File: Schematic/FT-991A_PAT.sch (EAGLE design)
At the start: 30 parts, among them Q1 PE4259, Q2 MC78L09ABDR2GOSCT, Q5 NCP553, Q7 J310, Q8 5086, X1 IF_IN, X2 SCP_OUT, X3 SDR_OUT

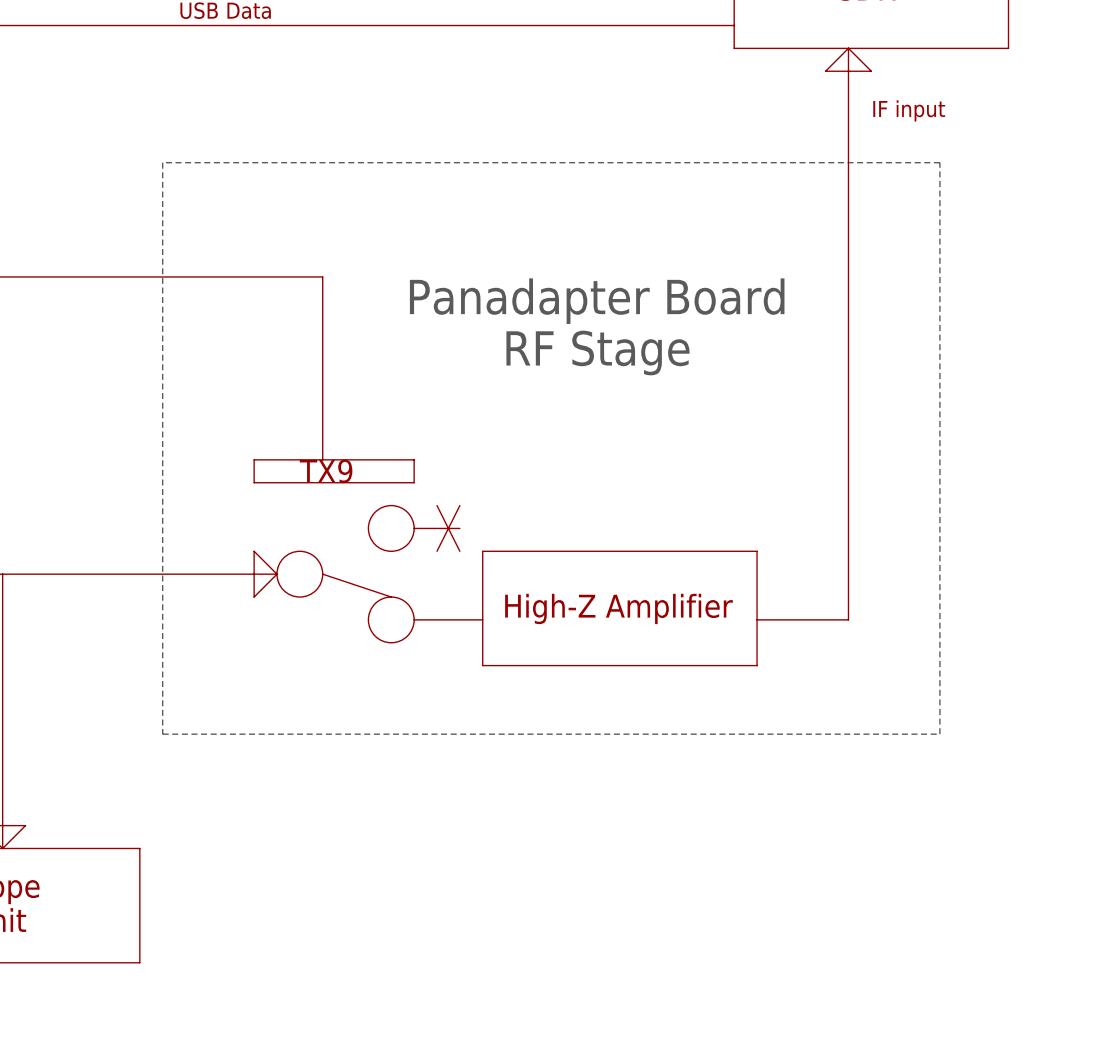
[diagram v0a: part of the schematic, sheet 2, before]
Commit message: Christening Rev. R
* New PDF files
* Voltage regulator re-routing
* Larger NCP533 and Diode pads
* Fixed some BOM errors
* Removed some old files
* Added Eagle Library file
* Fixed Readme links
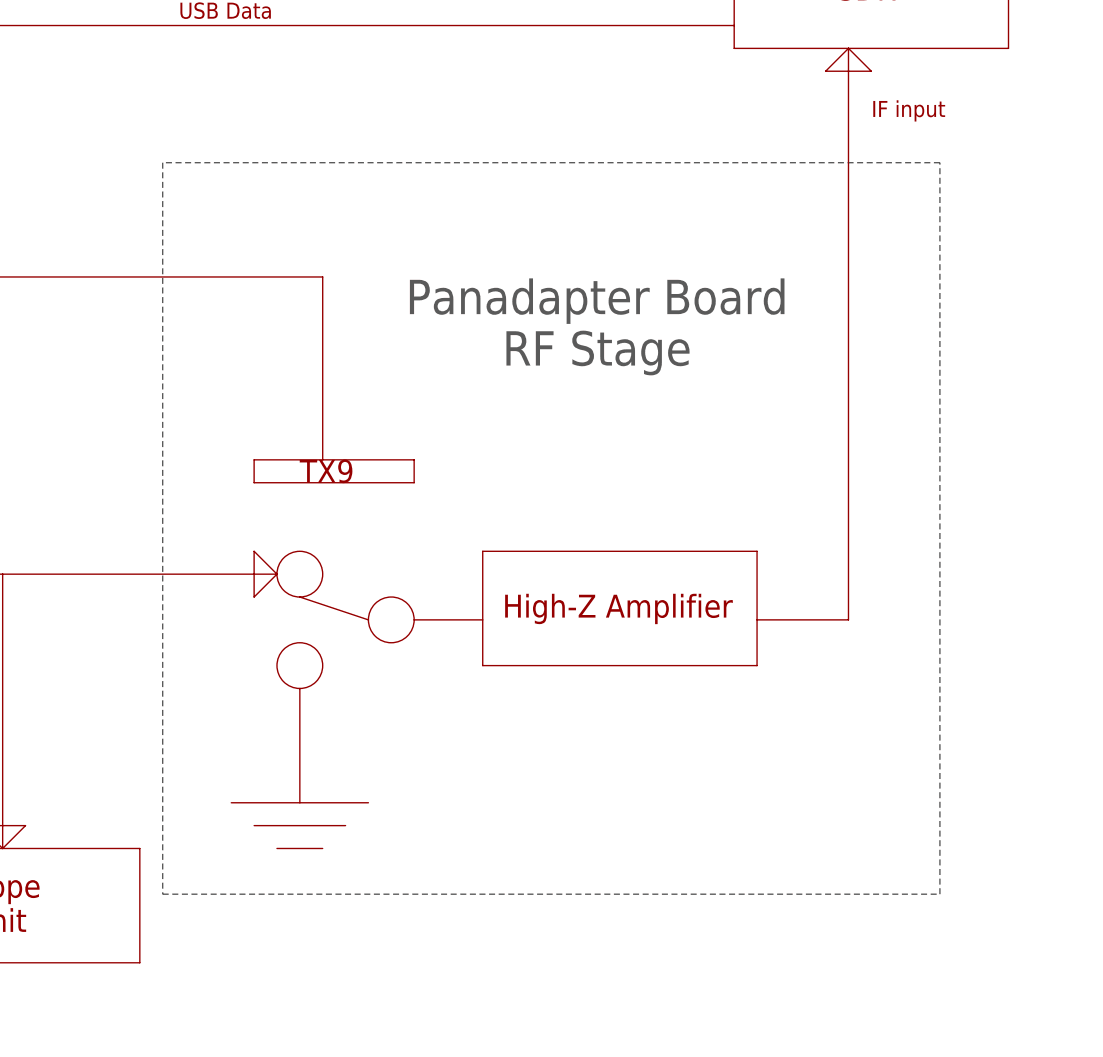
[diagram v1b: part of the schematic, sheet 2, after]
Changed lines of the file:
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@@
 <wire x1="147.32" y1="40.64" x2="116.84" y2="40.64" width="0.1524" layer="94"/>
 <wire x1="116.84" y1="40.64" x2="116.84" y2="53.34" width="0.1524" layer="94"/>
-<circle x="175.26" y="88.9" radius="2.54" width="0.1524" layer="94"/>
+<circle x="165.1" y="73.66" radius="2.54" width="0.1524" layer="94"/>
 <circle x="106.68" y="83.82" radius="15.450215625" width="0.1524" layer="94"/>
 <wire x1="96.52" y1="93.98" x2="116.84" y2="73.66" width="0.1524" layer="94"/>
@@
 <wire x1="91.44" y1="200.66" x2="182.88" y2="200.66" width="0.1524" layer="97" style="shortdash"/>
 <text x="127.762" y="174.244" size="3.81" layer="97">Main Unit</text>
-<wire x1="236.22" y1="66.04" x2="236.22" y2="129.54" width="0.1524" layer="97" style="shortdash"/>
-<wire x1="149.86" y1="129.54" x2="149.86" y2="66.04" width="0.1524" layer="97" style="shortdash"/>
-<wire x1="149.86" y1="66.04" x2="236.22" y2="66.04" width="0.1524" layer="97" style="shortdash"/>
+<wire x1="236.22" y1="48.26" x2="236.22" y2="129.54" width="0.1524" layer="97" style="shortdash"/>
+<wire x1="149.86" y1="129.54" x2="149.86" y2="48.26" width="0.1524" layer="97" style="shortdash"/>
+<wire x1="149.86" y1="48.26" x2="236.22" y2="48.26" width="0.1524" layer="97" style="shortdash"/>
 <text x="198.12" y="111.76" size="3.81" layer="97" align="center">Panadapter Board
 RF Stage</text>
@@
 <wire x1="226.06" y1="142.24" x2="226.06" y2="78.74" width="0.1524" layer="94"/>
 <wire x1="226.06" y1="78.74" x2="215.9" y2="78.74" width="0.1524" layer="94"/>
-<wire x1="177.8" y1="88.9" x2="182.88" y2="88.9" width="0.1524" layer="94"/>
-<wire x1="180.34" y1="91.44" x2="182.88" y2="86.36" width="0.1524" layer="94"/>
-<wire x1="180.34" y1="86.36" x2="182.88" y2="91.44" width="0.1524" layer="94"/>
-<wire x1="167.64" y1="83.82" x2="175.26" y2="81.28" width="0.1524" layer="94"/>
+<wire x1="172.72" y1="78.74" x2="165.1" y2="81.28" width="0.1524" layer="94"/>
+<wire x1="165.1" y1="71.12" x2="165.1" y2="58.42" width="0.1524" layer="94"/>
+<wire x1="157.48" y1="58.42" x2="172.72" y2="58.42" width="0.1524" layer="94"/>
+<wire x1="160.02" y1="55.88" x2="170.18" y2="55.88" width="0.1524" layer="94"/>
+<wire x1="162.56" y1="53.34" x2="167.64" y2="53.34" width="0.1524" layer="94"/>
 </plain>
 <instances>

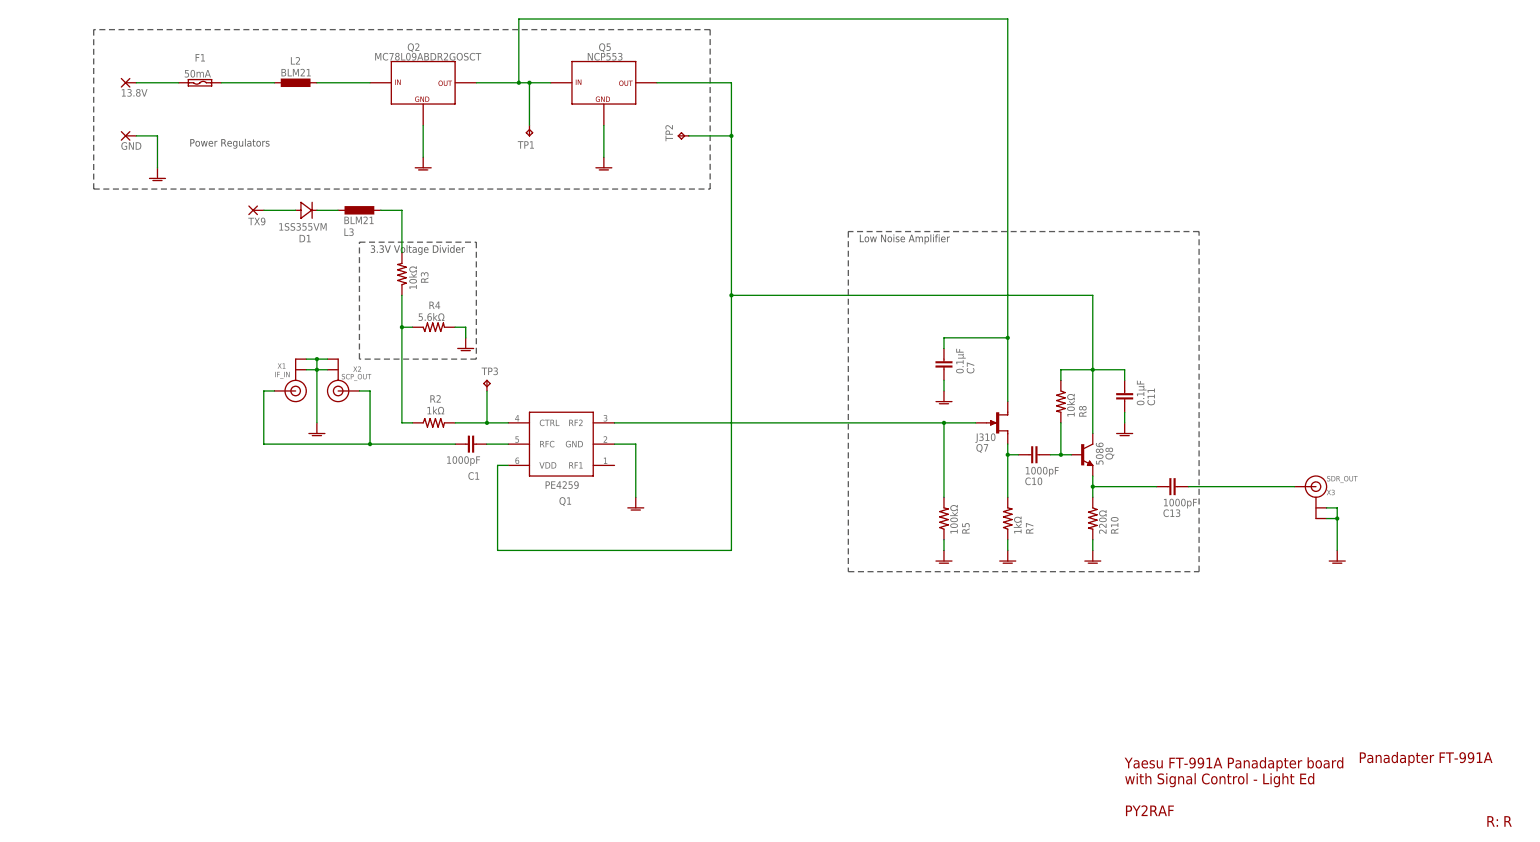
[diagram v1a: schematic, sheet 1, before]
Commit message: Announcing: Rev. S
* Replaced 2SC5086 with BFR193F amplifier, since 2SC5086 is now EOL
* Added a RF choke (L1) to avoid signal feedback propagating in 3V line
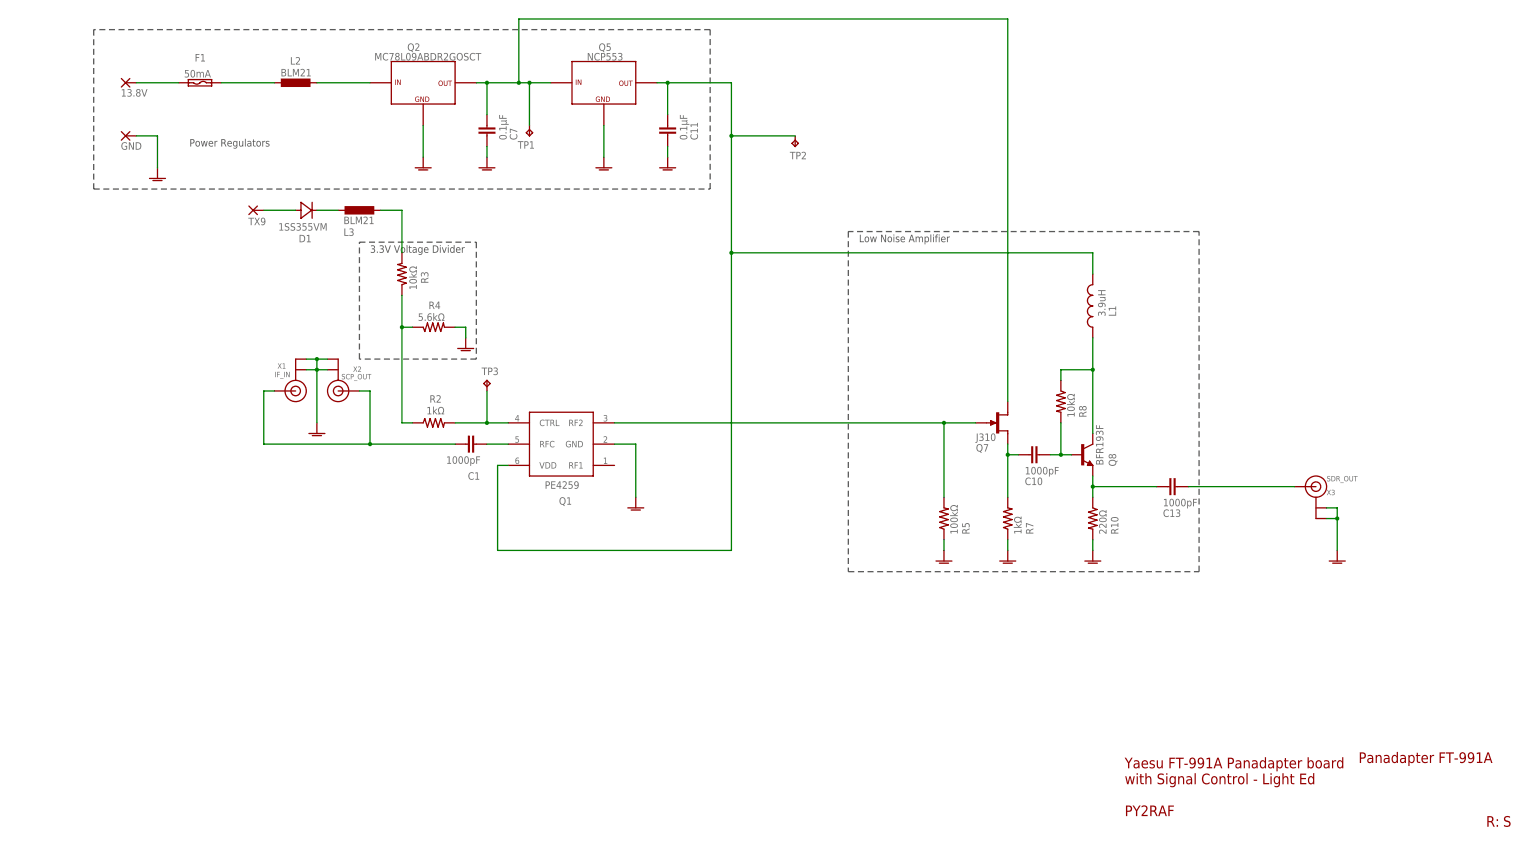
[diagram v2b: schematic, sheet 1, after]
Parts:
- added L1: 3.9uH, aarf:L-0805
- Q8: value 5086 -> BFR193F; device aarf:2SC5086 -> aarf:BFR193F
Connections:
- new net FB-3V: L1.2, Q8.C, R8.1
- net 3V: now also L1.1; no longer Q8.C, R8.1
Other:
- moved on the sheet: C11, C7, TP2
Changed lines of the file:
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@@
 <attribute name="PROJECT_INFO" value="Yaesu FT-991A Panadapter with Signal Control"/>
 <attribute name="PROJECT_NAME" value="FT-991A PAT &amp; SDR"/>
-<attribute name="REVISION_ID" value="R"/>
+<attribute name="REVISION_ID" value="S"/>
 </attributes>
 <variantdefs>
@@
 <parts>
 <part name="R5" library="aarf" deviceset="R-1206" device="" value="100kΩ"/>
-<part name="Q8" library="aarf" deviceset="2SC5086" device="" value="5086"/>
+<part name="Q8" library="aarf" deviceset="BFR193F" device="" value="BFR193F"/>
 <part name="R7" library="aarf" deviceset="R-1206" device="" value="1kΩ"/>
 <part name="C10" library="aarf" deviceset="C-0805" device="" value="1000pF"/>
@@
 <part name="GND" library="wirepad" library_urn="urn:adsk.eagle:library:412" deviceset="WIREPAD" device="SMD1,27-254" package3d_urn="urn:adsk.eagle:package:30839/1" value="GND"/>
 <part name="GND3" library="supply1" library_urn="urn:adsk.eagle:library:371" deviceset="GNDA" device=""/>
+<part name="L1" library="aarf" deviceset="L-0805" device="" value="3.9uH"/>
 </parts>
 <sheets>
@@
 </instance>
 <instance part="Q8" gate="G$1" x="279.4" y="93.98" smashed="yes">
-<attribute name="NAME" x="286.766" y="92.71" size="1.778" layer="95" rot="R90"/>
+<attribute name="NAME" x="287.528" y="91.186" size="1.778" layer="95" rot="R90"/>
 <attribute name="VALUE" x="284.48" y="91.44" size="1.778" layer="96" rot="R90"/>
 </instance>
@@
 </instance>
 <instance part="GND11" gate="1" x="246.38" y="68.58" smashed="yes"/>
-<instance part="C7" gate="G$1" x="246.38" y="116.84" smashed="yes">
-<attribute name="NAME" x="253.619" y="113.284" size="1.778" layer="95" rot="R90"/>
-<attribute name="VALUE" x="251.079" y="113.284" size="1.778" layer="96" rot="R90"/>
-</instance>
-<instance part="GND10" gate="1" x="246.38" y="106.68" smashed="yes"/>
-<instance part="C11" gate="G$1" x="289.56" y="109.22" smashed="yes">
-<attribute name="NAME" x="296.799" y="105.664" size="1.778" layer="95" rot="R90"/>
-<attribute name="VALUE" x="294.259" y="105.664" size="1.778" layer="96" rot="R90"/>
+<instance part="C7" gate="G$1" x="137.16" y="172.72" smashed="yes">
+<attribute name="NAME" x="144.399" y="169.164" size="1.778" layer="95" rot="R90"/>
+<attribute name="VALUE" x="141.859" y="169.164" size="1.778" layer="96" rot="R90"/>
+</instance>
+<instance part="GND10" gate="1" x="137.16" y="162.56" smashed="yes"/>
+<instance part="C11" gate="G$1" x="180.34" y="172.72" smashed="yes">
+<attribute name="NAME" x="187.579" y="169.164" size="1.778" layer="95" rot="R90"/>
+<attribute name="VALUE" x="185.039" y="169.164" size="1.778" layer="96" rot="R90"/>
 </instance>
 <instance part="R8" gate="G$1" x="274.32" y="106.68" smashed="yes" rot="R270">
@@
 <attribute name="VALUE" x="277.622" y="102.87" size="1.778" layer="96" rot="R90"/>
 </instance>
-<instance part="GND19" gate="1" x="289.56" y="99.06" smashed="yes"/>
+<instance part="GND19" gate="1" x="180.34" y="162.56" smashed="yes"/>
 <instance part="GND13" gate="1" x="261.62" y="68.58" smashed="yes"/>
 <instance part="R10" gate="G$1" x="281.94" y="78.74" smashed="yes" rot="R270">
@@
 <attribute name="TP_SIGNAL_NAME" x="146.05" y="171.45" size="1.778" layer="97" rot="R180"/>
 </instance>
-<instance part="TP2" gate="G$1" x="182.88" y="170.18" smashed="yes" rot="R90">
-<attribute name="NAME" x="181.61" y="168.91" size="1.778" layer="95" rot="R90"/>
-<attribute name="TP_SIGNAL_NAME" x="184.15" y="171.45" size="1.778" layer="97" rot="R90"/>
+<instance part="TP2" gate="G$1" x="210.82" y="167.64" smashed="yes" rot="MR180">
+<attribute name="NAME" x="209.55" y="166.37" size="1.778" layer="95" rot="MR180"/>
+<attribute name="TP_SIGNAL_NAME" x="212.09" y="168.91" size="1.778" layer="97" rot="MR180"/>
 </instance>
 <instance part="TP3" gate="G$1" x="137.16" y="111.76" smashed="yes">
@@
 </instance>
 <instance part="GND3" gate="1" x="58.42" y="160.02" smashed="yes"/>
+<instance part="L1" gate="G$1" x="281.94" y="129.54" smashed="yes" rot="MR0">
+<attribute name="NAME" x="285.75" y="127" size="1.778" layer="95" rot="MR90"/>
+<attribute name="VALUE" x="283.21" y="127" size="1.778" layer="96" rot="MR90"/>
+</instance>
 </instances>
 <busses>
@@
 <pinref part="GND19" gate="1" pin="GNDA"/>
 <pinref part="C11" gate="G$1" pin="2"/>
-<wire x1="289.56" y1="101.6" x2="289.56" y2="104.14" width="0.1524" layer="91"/>
+<wire x1="180.34" y1="165.1" x2="180.34" y2="167.64" width="0.1524" layer="91"/>
 </segment>
 <segment>
@@
 <pinref part="C7" gate="G$1" pin="2"/>
 <pinref part="GND10" gate="1" pin="GNDA"/>
-<wire x1="246.38" y1="111.76" x2="246.38" y2="109.22" width="0.1524" layer="91"/>
+<wire x1="137.16" y1="167.64" x2="137.16" y2="165.1" width="0.1524" layer="91"/>
 </segment>
 <segment>
@@
 <segment>
 <pinref part="C7" gate="G$1" pin="1"/>
-<wire x1="261.62" y1="121.92" x2="246.38" y2="121.92" width="0.1524" layer="91"/>
-<wire x1="246.38" y1="121.92" x2="246.38" y2="119.38" width="0.1524" layer="91"/>
 <pinref part="Q7" gate="G$1" pin="S"/>
-<wire x1="261.62" y1="106.68" x2="261.62" y2="121.92" width="0.1524" layer="91"/>
-<junction x="261.62" y="121.92"/>
 <wire x1="144.78" y1="198.12" x2="261.62" y2="198.12" width="0.1524" layer="91"/>
 <pinref part="Q5" gate="G$1" pin="IN"/>
 <pinref part="Q2" gate="G$1" pin="OUT"/>
-<wire x1="134.62" y1="182.88" x2="144.78" y2="182.88" width="0.1524" layer="91"/>
+<wire x1="134.62" y1="182.88" x2="137.16" y2="182.88" width="0.1524" layer="91"/>
+<wire x1="137.16" y1="182.88" x2="144.78" y2="182.88" width="0.1524" layer="91"/>
 <wire x1="144.78" y1="182.88" x2="147.32" y2="182.88" width="0.1524" layer="91"/>
 <wire x1="147.32" y1="182.88" x2="152.4" y2="182.88" width="0.1524" layer="91"/>
@@
 <wire x1="147.32" y1="172.72" x2="147.32" y2="182.88" width="0.1524" layer="91"/>
 <junction x="147.32" y="182.88"/>
-<wire x1="261.62" y1="121.92" x2="261.62" y2="198.12" width="0.1524" layer="91"/>
+<wire x1="261.62" y1="106.68" x2="261.62" y2="198.12" width="0.1524" layer="91"/>
+<wire x1="137.16" y1="175.26" x2="137.16" y2="182.88" width="0.1524" layer="91"/>
+<junction x="137.16" y="182.88"/>
 </segment>
 </net>
 <net name="3V" class="0">
 <segment>
-<wire x1="195.58" y1="71.12" x2="195.58" y2="132.08" width="0.1524" layer="91"/>
+<wire x1="195.58" y1="71.12" x2="195.58" y2="142.24" width="0.1524" layer="91"/>
 <pinref part="Q5" gate="G$1" pin="OUT"/>
-<wire x1="195.58" y1="132.08" x2="195.58" y2="170.18" width="0.1524" layer="91"/>
+<wire x1="195.58" y1="142.24" x2="195.58" y2="170.18" width="0.1524" layer="91"/>
 <wire x1="195.58" y1="170.18" x2="195.58" y2="182.88" width="0.1524" layer="91"/>
-<wire x1="177.8" y1="182.88" x2="195.58" y2="182.88" width="0.1524" layer="91"/>
+<wire x1="177.8" y1="182.88" x2="180.34" y2="182.88" width="0.1524" layer="91"/>
 <pinref part="Q1" gate="G$1" pin="VDD"/>
+<wire x1="180.34" y1="182.88" x2="195.58" y2="182.88" width="0.1524" layer="91"/>
 <wire x1="142.24" y1="91.44" x2="139.7" y2="91.44" width="0.1524" layer="91"/>
 <wire x1="139.7" y1="91.44" x2="139.7" y2="71.12" width="0.1524" layer="91"/>
 <wire x1="139.7" y1="71.12" x2="195.58" y2="71.12" width="0.1524" layer="91"/>
 <pinref part="TP2" gate="G$1" pin="TP"/>
-<wire x1="185.42" y1="170.18" x2="195.58" y2="170.18" width="0.1524" layer="91"/>
+<wire x1="210.82" y1="170.18" x2="195.58" y2="170.18" width="0.1524" layer="91"/>
 <junction x="195.58" y="170.18"/>
+<wire x1="281.94" y1="142.24" x2="195.58" y2="142.24" width="0.1524" layer="91"/>
+<junction x="195.58" y="142.24"/>
+<wire x1="281.94" y1="137.16" x2="281.94" y2="142.24" width="0.1524" layer="91"/>
+<pinref part="L1" gate="G$1" pin="1"/>
+<pinref part="C11" gate="G$1" pin="1"/>
+<wire x1="180.34" y1="182.88" x2="180.34" y2="175.26" width="0.1524" layer="91"/>
+<junction x="180.34" y="182.88"/>
+</segment>
+</net>
+<net name="FB-3V" class="0">
+<segment>
 <pinref part="Q8" gate="G$1" pin="C"/>
-<pinref part="C11" gate="G$1" pin="1"/>
-<wire x1="289.56" y1="114.3" x2="289.56" y2="111.76" width="0.1524" layer="91"/>
 <pinref part="R8" gate="G$1" pin="1"/>
 <wire x1="274.32" y1="111.76" x2="274.32" y2="114.3" width="0.1524" layer="91"/>
 <wire x1="274.32" y1="114.3" x2="281.94" y2="114.3" width="0.1524" layer="91"/>
-<wire x1="281.94" y1="114.3" x2="289.56" y2="114.3" width="0.1524" layer="91"/>
 <junction x="281.94" y="114.3"/>
+<wire x1="281.94" y1="114.3" x2="281.94" y2="121.92" width="0.1524" layer="91"/>
 <wire x1="281.94" y1="114.3" x2="281.94" y2="99.06" width="0.1524" layer="91"/>
-<wire x1="281.94" y1="114.3" x2="281.94" y2="132.08" width="0.1524" layer="91"/>
-<wire x1="281.94" y1="132.08" x2="195.58" y2="132.08" width="0.1524" layer="91"/>
-<junction x="195.58" y="132.08"/>
-</segment>
-</net>
+<pinref part="L1" gate="G$1" pin="2"/>
+</segment>
+</net>
